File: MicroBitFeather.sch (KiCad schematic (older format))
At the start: 3 parts

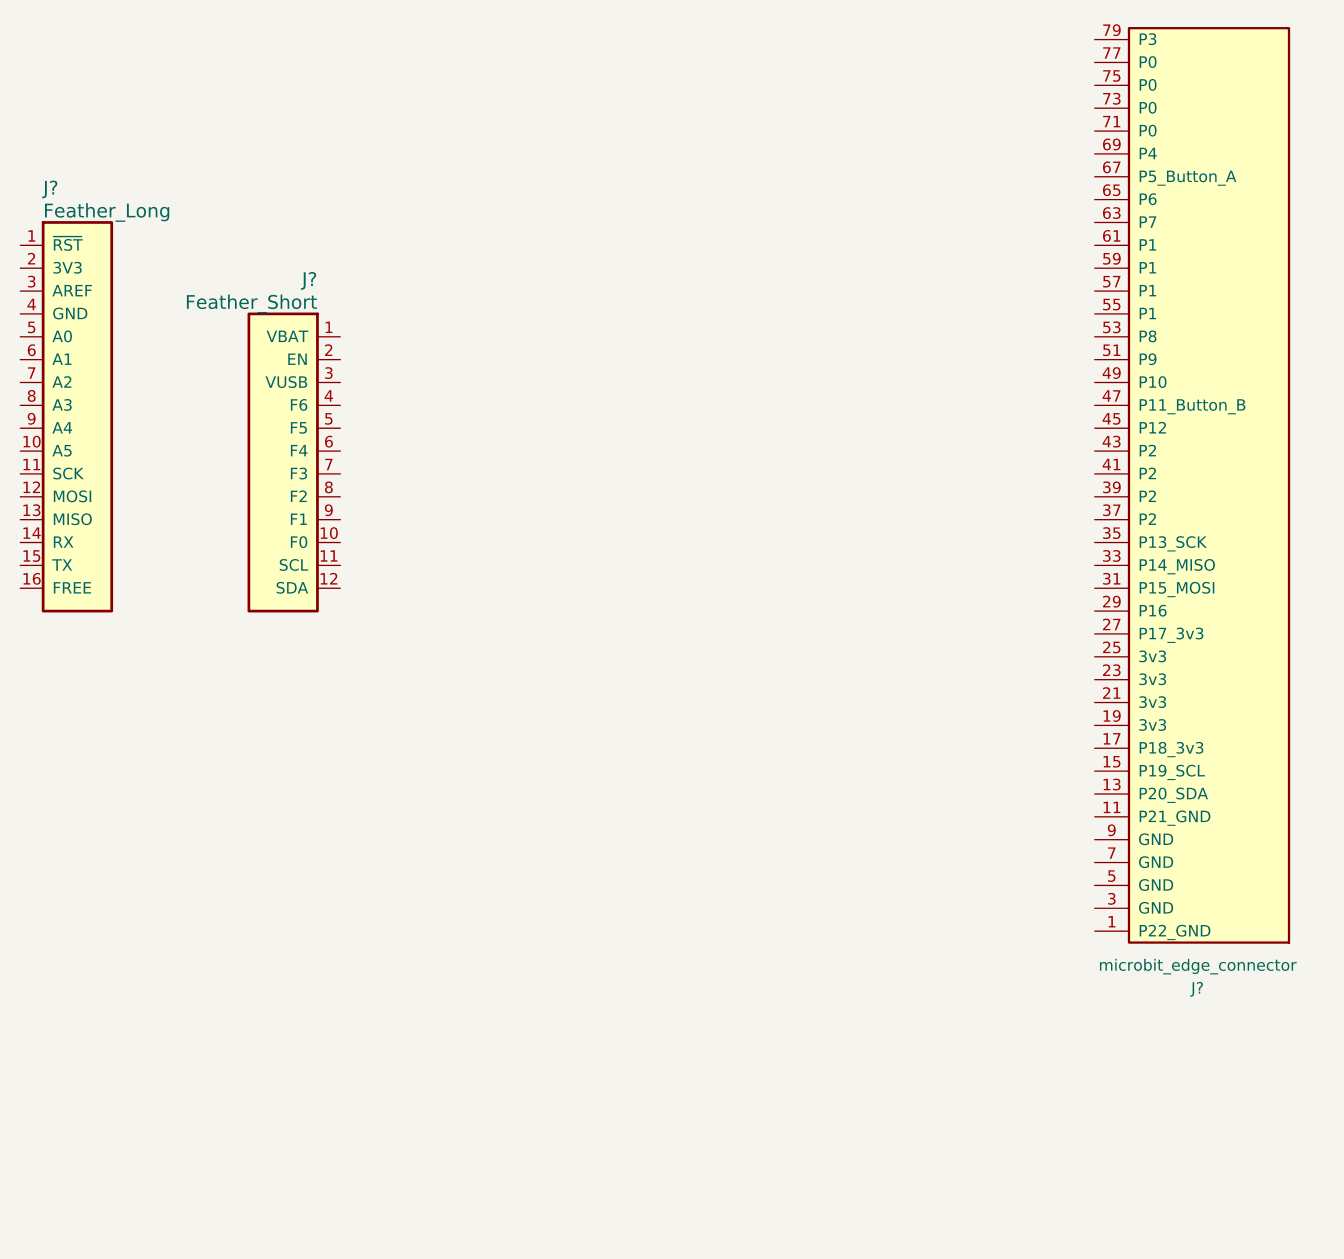
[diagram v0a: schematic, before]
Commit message: Wire up the micro:bit and feather connectors.
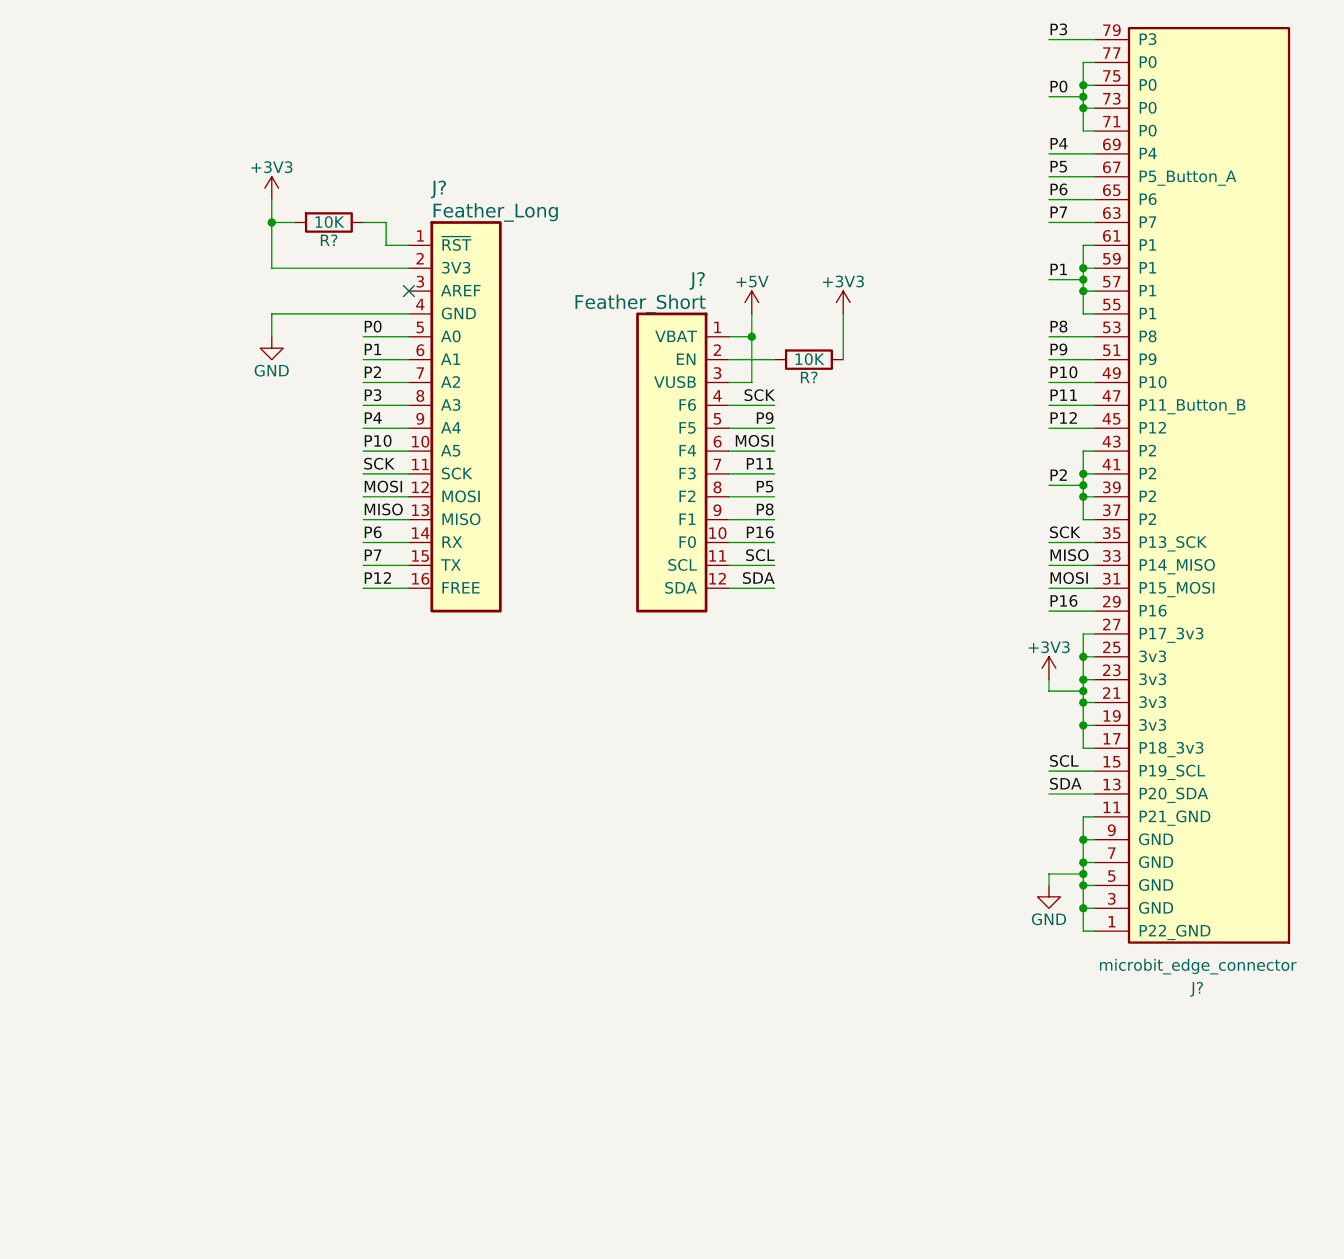
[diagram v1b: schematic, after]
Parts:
- added R? (x2): 10K, symbol R
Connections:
- net GND: now reaches J?.1 (P22_GND)
- net GND: now also J?.11 (P21_GND), J?.3 (GND), J?.4 (GND), J?.5 (GND), J?.7 (GND), J?.9 (GND)
- net SDA: now reaches J?.13 (P20_SDA)
- net SDA: now also J?.12 (SDA)
- net SCL: now reaches J?.15 (P19_SCL)
- net SCL: now also J?.11 (SCL)
- net +3V3: now reaches J?.17 (P18_3v3)
- net +3V3: now also J?.19 (3v3), J?.2 (3V3), J?.21 (3v3), J?.23 (3v3), J?.25 (3v3), J?.27 (P17_3v3), R?.1, R?.2
- net P16: now reaches J?.29 (P16)
- net P16: now also J?.10 (F0)
- net MOSI: now reaches J?.31 (P15_MOSI)
- net MOSI: now also J?.12 (MOSI), J?.6 (F4)
- net MISO: now reaches J?.33 (P14_MISO)
- net MISO: now also J?.13 (MISO)
- net SCK: now reaches J?.35 (P13_SCK)
- net SCK: now also J?.11 (SCK), J?.4 (F6)
- net P2: now reaches J?.37 (P2)
- net P2: now also J?.39 (P2), J?.41 (P2), J?.43 (P2), J?.7 (A2)
- net P12: now reaches J?.45 (P12)
- net P12: now also J?.16 (FREE)
- net P11: now reaches J?.47 (P11_Button_B)
- net P11: now also J?.7 (F3)
- net P10: now reaches J?.49 (P10)
- net P10: now also J?.10 (A5)
- net P9: now reaches J?.51 (P9)
- net P9: now also J?.5 (F5)
- net P8: now reaches J?.53 (P8)
- net P8: now also J?.9 (F1)
- net P1: now reaches J?.55 (P1)
- net P1: now also J?.57 (P1), J?.59 (P1), J?.6 (A1), J?.61 (P1)
- net P7: now reaches J?.63 (P7)
- net P7: now also J?.15 (TX)
- net P6: now reaches J?.65 (P6)
- net P6: now also J?.14 (RX)
- net P5: now reaches J?.67 (P5_Button_A)
- net P5: now also J?.8 (F2)
- net P4: now reaches J?.69 (P4)
- net P4: now also J?.9 (A4)
- net P0: now reaches J?.71 (P0)
- net P0: now also J?.5 (A0), J?.73 (P0), J?.75 (P0), J?.77 (P0)
- net P3: now reaches J?.79 (P3)
- net P3: now also J?.8 (A3)
- net at J?.1 (~RST): now also R?.1
- net +5V: now reaches J?.1 (VBAT)
- net +5V: now also J?.3 (VUSB)
- net at J?.2 (EN): now also R?.2
- no-connect marks 0 -> 1
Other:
- moved on the sheet: J?

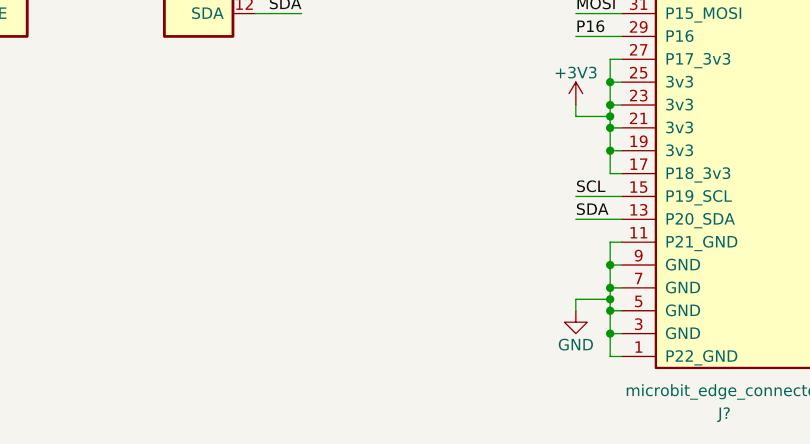
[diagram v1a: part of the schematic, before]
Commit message: Add connector for NeoPixels.
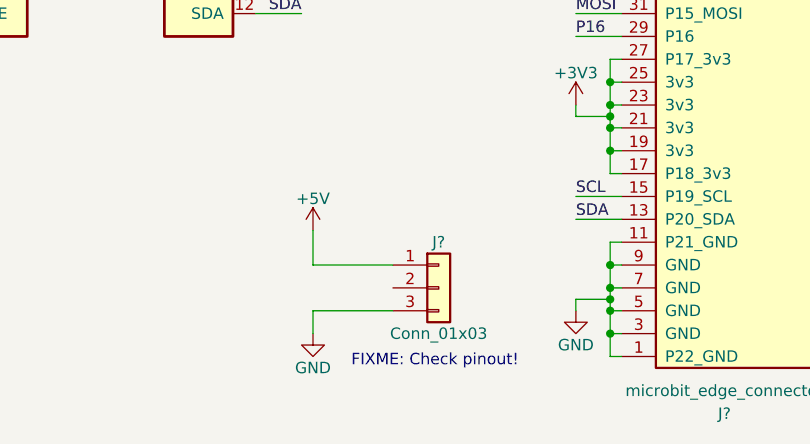
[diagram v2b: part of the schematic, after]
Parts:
- added J?: Conn_01x03, symbol Conn_01x03
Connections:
- net +5V: now also J?.1 (Pin_1)
- net GND: now also J?.3 (Pin_3)
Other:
- note added: "FIXME: Check pinout!"
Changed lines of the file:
@@
 Wire Wire Line
 	5600 3600 5800 3600
+$Comp
+L Conn_01x03 J?
+U 1 1 5B8792D8
+P 6400 4800
+F 0 "J?" H 6400 5000 50  0000 C CNN
+F 1 "Conn_01x03" H 6400 4600 50  0000 C CNN
+F 2 "" H 6400 4800 50  0001 C CNN
+F 3 "" H 6400 4800 50  0001 C CNN
+	1    6400 4800
+	1    0    0    -1
+$EndComp
+Text Notes 6750 5150 2    50   ~ 0
+FIXME: Check pinout!
+$Comp
+L GND #PWR?
+U 1 1 5B87949E
+P 5850 5000
+F 0 "#PWR?" H 5850 4750 50  0001 C CNN
+F 1 "GND" H 5850 4850 50  0000 C CNN
+F 2 "" H 5850 5000 50  0001 C CNN
+F 3 "" H 5850 5000 50  0001 C CNN
+	1    5850 5000
+	1    0    0    -1
+$EndComp
+$Comp
+L +5V #PWR?
+U 1 1 5B8794C4
+P 5850 4550
+F 0 "#PWR?" H 5850 4400 50  0001 C CNN
+F 1 "+5V" H 5850 4690 50  0000 C CNN
+F 2 "" H 5850 4550 50  0001 C CNN
+F 3 "" H 5850 4550 50  0001 C CNN
+	1    5850 4550
+	1    0    0    -1
+$EndComp
+Wire Wire Line
+	5850 4550 5850 4700
+Wire Wire Line
+	5850 4700 6200 4700
+Wire Wire Line
+	5850 5000 5850 4900
+Wire Wire Line
+	5850 4900 6200 4900
 $EndSCHEMATC

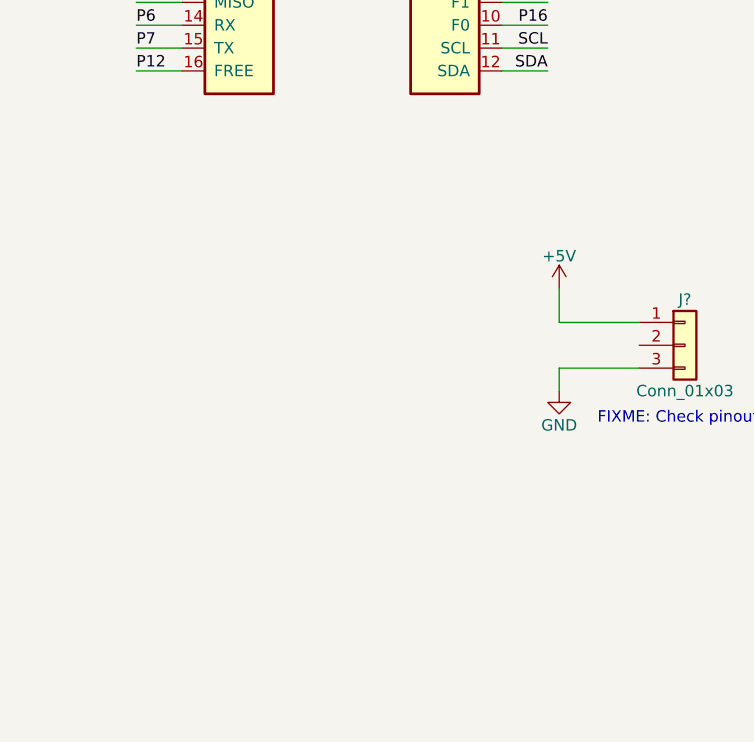
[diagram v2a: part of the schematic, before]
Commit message: Align 74AHCT125 pins to grid.
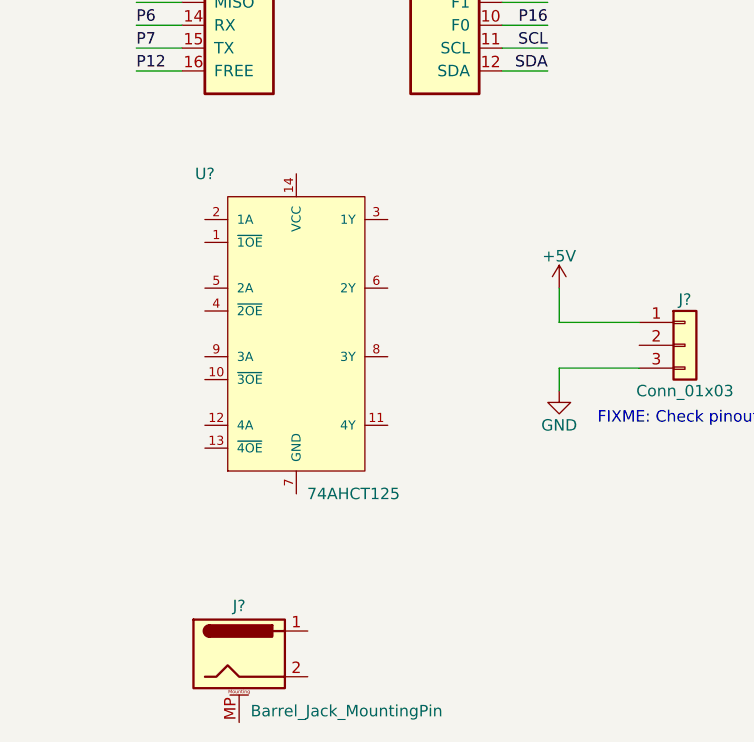
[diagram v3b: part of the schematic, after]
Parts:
- added J?: Barrel_Jack_MountingPin, symbol Barrel_Jack_MountingPin
- added U?: 74AHCT125, symbol 74AHCT125
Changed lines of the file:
@@
 LIBS:feather
 LIBS:lib_microbit_connector
+LIBS:misc_lib
 LIBS:MicroBitFeather-cache
 EELAYER 25 0
@@
 Wire Wire Line
 	5850 4900 6200 4900
+$Comp
+L 74AHCT125 U?
+U 1 1 5B8786B5
+P 4700 4750
+F 0 "U?" H 4300 5450 50  0000 C CNN
+F 1 "74AHCT125" H 4950 4050 50  0000 C CNN
+F 2 "" H 4700 4750 60  0000 C CNN
+F 3 "" H 4700 4750 60  0000 C CNN
+	1    4700 4750
+	1    0    0    -1
+$EndComp
+$Comp
+L Barrel_Jack_MountingPin J?
+U 1 1 5B8786E0
+P 4450 6150
+F 0 "J?" H 4450 6360 50  0000 C CNN
+F 1 "Barrel_Jack_MountingPin" H 4500 5900 50  0000 L CNN
+F 2 "" H 4500 6110 50  0001 C CNN
+F 3 "" H 4500 6110 50  0001 C CNN
+	1    4450 6150
+	1    0    0    -1
+$EndComp
 $EndSCHEMATC
